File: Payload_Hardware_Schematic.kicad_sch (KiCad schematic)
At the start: 0 parts

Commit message: test
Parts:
- added U1: STM32F411 BlackPill, WeAct_Black_Pill_V2.0:STM32F411_Black_Pill, symbol Payload-STM32:STM32F411_Black_Pill
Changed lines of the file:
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@@
 	(generator_version "9.0")
 	(paper "A4")
+	(symbol
+		(lib_id "Payload-STM32:STM32F411_Black_Pill")
+		(at 135.89 99.06 0)
+		(unit 1)
+		(exclude_from_sim no)
+		(in_bom yes)
+		(on_board yes)
+		(dnp no)
+		(fields_autoplaced yes)
+		(property "Reference" "U1"
+			(at 143.1133 125.73 0)
+			(effects
+				(font
+					(size 1.27 1.27)
+				)
+				(justify left)
+			)
+		)
+		(property "Value" "STM32F411 BlackPill"
+			(at 143.1133 128.27 0)
+			(effects
+				(font
+					(size 1.27 1.27)
+				)
+				(justify left)
+			)
+		)
+		(property "Footprint" "WeAct_Black_Pill_V2.0:STM32F411_Black_Pill"
+			(at 132.08 85.09 0)
+			(effects
+				(font
+					(size 1.27 1.27)
+				)
+				(hide yes)
+			)
+		)
+		(property "Datasheet" "https://docs.zephyrproject.org/latest/boards/arm/blackpill_f411ce/doc/index.html"
+			(at 132.08 85.09 0)
+			(effects
+				(font
+					(size 1.27 1.27)
+				)
+				(hide yes)
+			)
+		)
+		(property "Description" "WeAct Black Pill V2.0 development board, based STM32F411CE, made by Dony Setiawan"
+			(at 135.89 99.06 0)
+			(effects
+				(font
+					(size 1.27 1.27)
+				)
+				(hide yes)
+			)
+		)
+		(pin "9"
+		)
+		(pin "6"
+		)
+		(pin "38"
+		)
+		(pin "32"
+		)
+		(pin "7"
+		)
+		(pin "8"
+		)
+		(pin "34"
+		)
+		(pin "20"
+		)
+		(pin "14"
+		)
+		(pin "29"
+		)
+		(pin "19"
+		)
+		(pin "25"
+		)
+		(pin "13"
+		)
+		(pin "31"
+		)
+		(pin "21"
+		)
+		(pin "28"
+		)
+		(pin "30"
+		)
+		(pin "26"
+		)
+		(pin "27"
+		)
+		(pin "33"
+		)
+		(pin "5"
+		)
+		(pin "10"
+		)
+		(pin "18"
+		)
+		(pin "39"
+		)
+		(pin "40"
+		)
+		(pin "35"
+		)
+		(pin "36"
+		)
+		(pin "11"
+		)
+		(pin "12"
+		)
+		(pin "15"
+		)
+		(pin "16"
+		)
+		(pin "37"
+		)
+		(pin "22"
+		)
+		(pin "17"
+		)
+		(pin "2"
+		)
+		(pin "3"
+		)
+		(pin "23"
+		)
+		(pin "1"
+		)
+		(pin "4"
+		)
+		(pin "24"
+		)
+		(instances
+			(project ""
+				(path "/f4ead8bb-2437-4e54-a6d9-f5ca11bfd675"
+					(reference "U1")
+					(unit 1)
+				)
+			)
+		)
+	)
 	(sheet_instances
 		(path "/"

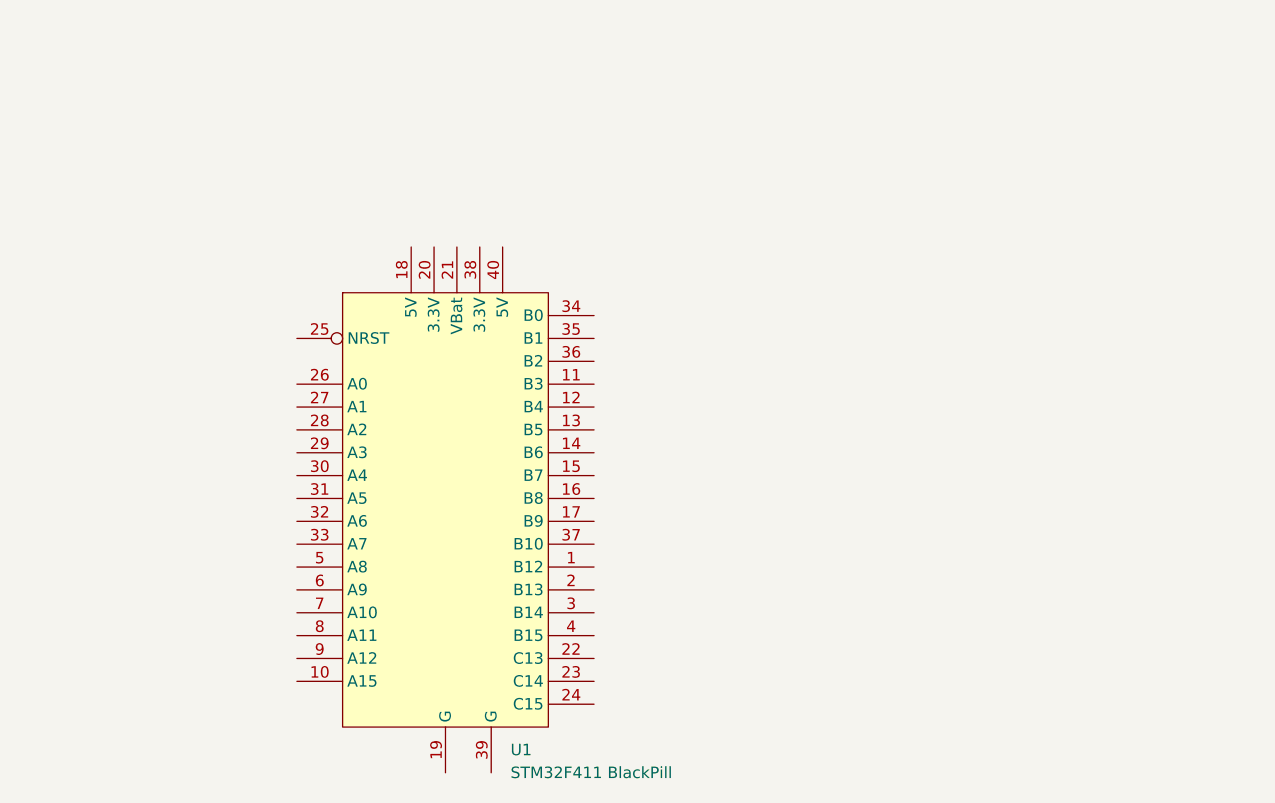
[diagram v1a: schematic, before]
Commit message: 3v3 and 5v buck converters added
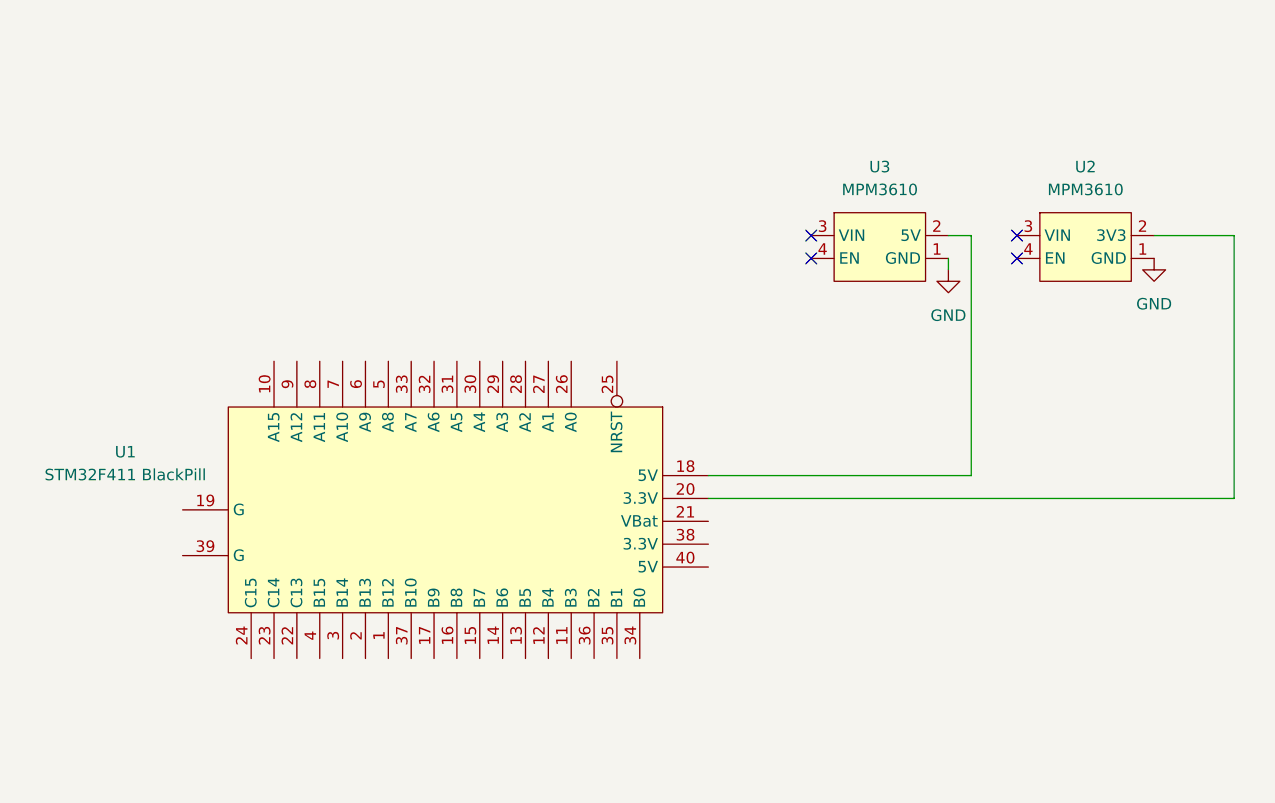
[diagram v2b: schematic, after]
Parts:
- added U2, U3: MPM3610, Footprints:MPM3610, symbol Avionics_Symbols:MPM3610
- U1: footprint WeAct_Black_Pill_V2.0:STM32F411_Black_Pill -> Payload-STM32:STM32F411_Black_Pill
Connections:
- net at U1.18 (5V): now also U3.2 (5V)
- net at U1.20 (3.3V): now also U2.2 (3V3)
- new net GND: U2.1 (GND), U3.1 (GND)
- no-connect marks 0 -> 4
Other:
- moved on the sheet: U1

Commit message: added pins
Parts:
- removed U1: STM32F411 BlackPill, Payload-STM32:STM32F411_Black_Pill, symbol Payload-STM32:STM32F411_Black_Pill
- added J1: Conn_01x08_Pin, symbol Connector:Conn_01x08_Pin
- added J2: Conn_01x06_Pin_5V, symbol Connector:Conn_01x06_Pin
- added J3: Conn_01x06_Pin_3V3, symbol Connector:Conn_01x06_Pin
- added J4: Conn_01x04_Pin, symbol Connector:Conn_01x04_Pin
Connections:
- net GND: now also J1.1 (Pin_1), J1.2 (Pin_2), J1.3 (Pin_3), J1.4 (Pin_4), J1.5 (Pin_5), J1.6 (Pin_6), J1.7 (Pin_7), J1.8 (Pin_8)
- net at U3.2 (5V): now also J2.1 (Pin_1), J2.2 (Pin_2), J2.3 (Pin_3), J2.4 (Pin_4), J2.5 (Pin_5), J2.6 (Pin_6)
- net +7.2V: now reaches U3.3 (VIN)
- net +7.2V: now also U2.3 (VIN), J4.1 (Pin_1), J4.2 (Pin_2), J4.3 (Pin_3), J4.4 (Pin_4)
- net at U2.2 (3V3): now also J3.1 (Pin_1), J3.2 (Pin_2), J3.3 (Pin_3), J3.4 (Pin_4), J3.5 (Pin_5), J3.6 (Pin_6)
- no-connect marks 4 -> 2
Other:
- moved on the sheet: U2, U3
